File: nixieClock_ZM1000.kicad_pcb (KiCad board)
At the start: 2 copper layers, 124.5 x 100.3 mm, 62 parts, among them J1 Conn_01x08_Female, J2 Conn_01x02_Female, J3 SPARE, Q1 BC547, Q2 BC547, Q3 BC547, Q4 BC547, Q5 BC547, Q6 BC547, Q7 Q_NMOS_GDS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

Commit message: 90% routed
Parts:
- moved J3 13.5 mm to (192.5, 113.8)
- moved R8 10.2 mm to (121.7, 82.5), turned to 90 degrees
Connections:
- U14 pad 1: /Shift Registers/BCD_T1B -> /Shift Registers/DP1
- U14 pad 15: /Shift Registers/BCD_T1A -> /Shift Registers/BCD_T2C
- U14 pad 2: /Shift Registers/BCD_T1C -> /Shift Registers/BCD_T1A
- U14 pad 4: /Shift Registers/DP1 -> /Shift Registers/BCD_T1B
- U14 pad 5: /Shift Registers/BCD_T2A -> /Shift Registers/BCD_T1C
- U14 pad 6: /Shift Registers/BCD_T2B -> /Shift Registers/BCD_T2A
- U14 pad 7: /Shift Registers/BCD_T2C -> /Shift Registers/BCD_T2B
- U15 pad 15: /Shift Registers/BCD_T2D -> /Shift Registers/BCD_T4A
- U15 pad 2: /Shift Registers/BCD_T3A -> /Shift Registers/BCD_T2D
- U15 pad 3: /Shift Registers/BCD_T3B -> /Shift Registers/BCD_T3C
- U15 pad 4: /Shift Registers/BCD_T3C -> /Shift Registers/BCD_T3B
- U15 pad 6: /Shift Registers/DP3 -> /Shift Registers/BCD_T3A
- U15 pad 7: /Shift Registers/BCD_T4A -> /Shift Registers/DP3
- U16 pad 1: /Shift Registers/BCD_T4C -> /Shift Registers/DP4
- U16 pad 15: /Shift Registers/BCD_T4B -> /Shift Registers/BCD_T5A
- U16 pad 3: /Shift Registers/DP4 -> /Shift Registers/BCD_T4B
- U16 pad 4: /Shift Registers/BCD_T5A -> /Shift Registers/BCD_T4C
- U16 pad 5: /Shift Registers/BCD_T5B -> /Shift Registers/BCD_T5C
- U16 pad 6: /Shift Registers/BCD_T5C -> /Shift Registers/BCD_T5B
- U17 pad 1: /Shift Registers/BCD_T6A -> /Shift Registers/DP5
- U17 pad 15: /Shift Registers/DP5 -> /Shift Registers/DP6
- U17 pad 2: /Shift Registers/BCD_T6B -> /Shift Registers/BCD_T6C
- U17 pad 3: /Shift Registers/BCD_T6C -> /Shift Registers/BCD_T6B
- U17 pad 5: /Shift Registers/DP6 -> /Shift Registers/BCD_T6A
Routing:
- net /Control/BLANK: track 45.8 -> 160.5 mm
- net /Control/5V: track 15.0 -> 128.7 mm, vias 0 -> 1
- net Net-(U2-Pad5): track 0.00 -> 51.2 mm
- net Net-(U4-Pad5): track 0.00 -> 51.2 mm
- net Net-(U10-Pad5): track 0.00 -> 51.2 mm
- net Net-(U3-Pad5): track 0.00 -> 51.2 mm
- net /PSU/HV: track 0.00 -> 51.1 mm
- net Net-(U11-Pad8): track 0.00 -> 51.1 mm
- net Net-(U12-Pad8): track 0.00 -> 51.0 mm
- net /Shift Registers/BCD_T4A: track 0.00 -> 40.3 mm
- net /Shift Registers/BCD_T2A: track 0.00 -> 39.6 mm
- net /Shift Registers/BCD_T5D: track 0.00 -> 37.1 mm
- net /Shift Registers/BCD_T2D: track 0.00 -> 36.5 mm
- net Net-(U12-Pad1): track 0.00 -> 36.1 mm
- net Net-(U3-Pad11): track 0.00 -> 36.1 mm
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- added copper zone on B.Cu, net GND

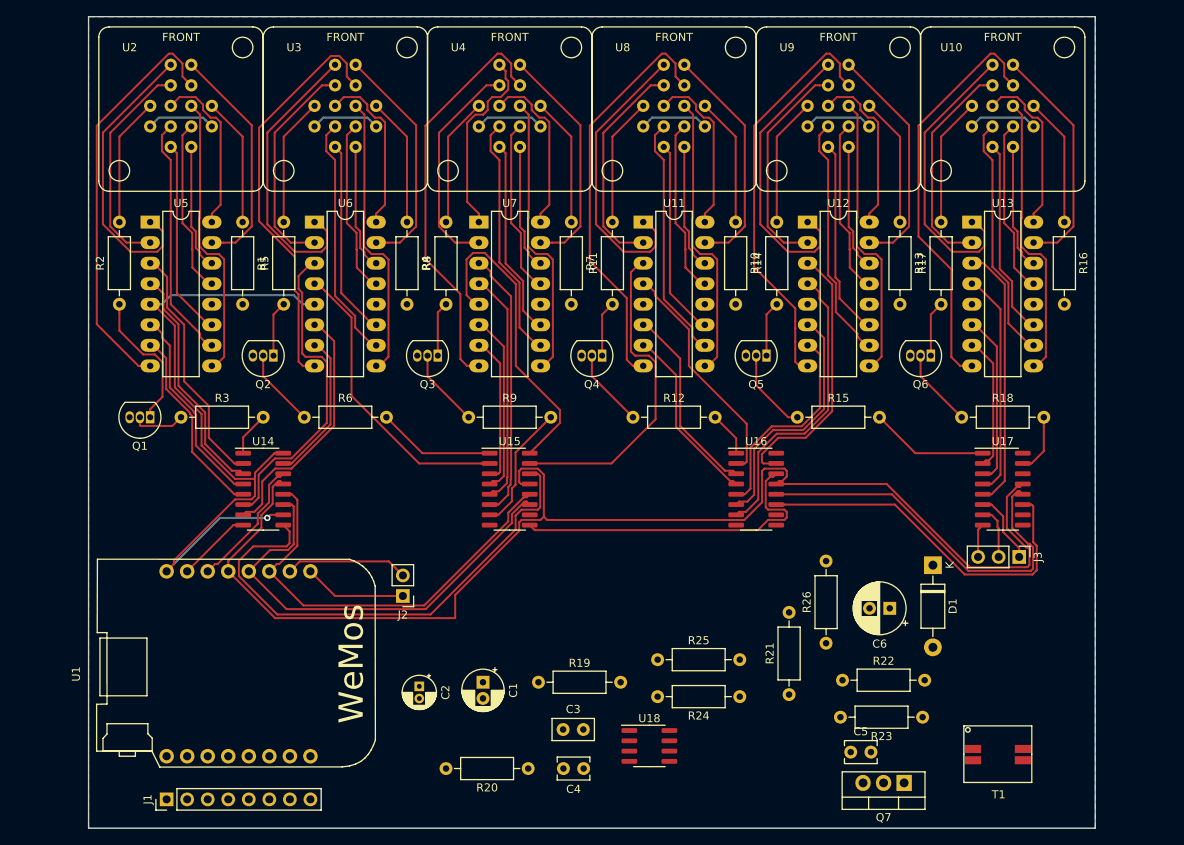
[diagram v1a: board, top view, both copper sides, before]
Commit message: Completed layout inc optimisation of data pattern for shift registers
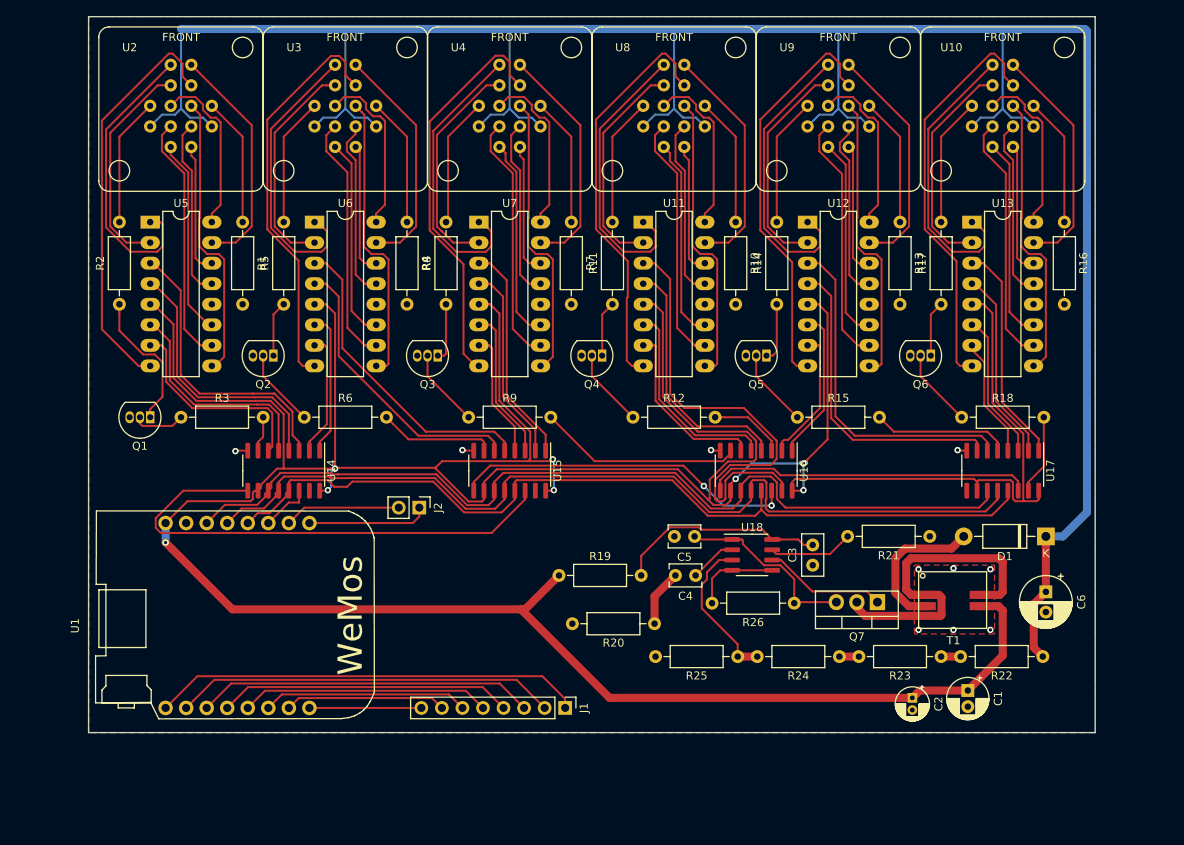
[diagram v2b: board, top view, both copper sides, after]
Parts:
- removed J3: SPARE, Connector_PinHeader_2.54mm:PinHeader_1x03_P2.54mm_Vertical
- moved C2 61.0 mm to (179.3, 131.2)
- moved C1 60.0 mm to (186.2, 130.3)
- moved J1 50.6 mm to (136.4, 132.5), turned to 270 degrees
- moved C3 37.0 mm to (167.0, 114.8), turned to 90 degrees
- moved C5 32.9 mm to (152.4, 111.3), turned to 180 degrees
- moved C4 27.6 mm to (152.5, 116.1)
- moved U18 26.8 mm to (159.5, 113.5)
- moved R21 26.2 mm to (181.5, 111.3), turned to 180 degrees
- moved R22 24.9 mm to (195.5, 126.1), turned to 180 degrees
- moved R20 23.8 mm to (147.4, 122.0)
- moved Q7 22.6 mm to (175.0, 119.4)
- moved T1 19.9 mm to (184.4, 119.1)
- moved C6 19.4 mm to (195.8, 118.1), turned to 270 degrees
- moved D1 14.4 mm to (195.8, 111.3), turned to 180 degrees
- moved R19 13.5 mm to (135.6, 116.1)
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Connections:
- U1 pad 3: /Control/TUBETX -> /Control/SHIFTCLK
- U1 pad 4: /Control/BLANK -> /Control/STORAGECLK
- U1 pad 5: /Control/SHIFTCLK -> /Control/BLANK
- U1 pad 6: /Control/STORAGECLK -> /Control/TUBETX
- U14 pad 1: /Shift Registers/DP1 -> /Shift Registers/BCD_T2B
- U14 pad 15: /Shift Registers/BCD_T2C -> Net-(U14-Pad15)
- U14 pad 2: /Shift Registers/BCD_T1A -> /Shift Registers/BCD_T2C
- U14 pad 3: /Shift Registers/BCD_T1D -> /Shift Registers/BCD_T1A
- U14 pad 4: /Shift Registers/BCD_T1B -> /Shift Registers/BCD_T1D
- U14 pad 5: /Shift Registers/BCD_T1C -> /Shift Registers/BCD_T1B
- U14 pad 6: /Shift Registers/BCD_T2A -> /Shift Registers/BCD_T1C
- U14 pad 7: /Shift Registers/BCD_T2B -> /Shift Registers/DP1
- U15 pad 1: /Shift Registers/DP2 -> /Shift Registers/BCD_T3A
- U15 pad 15: /Shift Registers/BCD_T4A -> Net-(U15-Pad15)
- U15 pad 2: /Shift Registers/BCD_T2D -> /Shift Registers/BCD_T3D
- U15 pad 3: /Shift Registers/BCD_T3C -> /Shift Registers/BCD_T3B
- U15 pad 4: /Shift Registers/BCD_T3B -> /Shift Registers/BCD_T3C
- U15 pad 5: /Shift Registers/BCD_T3D -> /Shift Registers/BCD_T2A
- U15 pad 6: /Shift Registers/BCD_T3A -> /Shift Registers/BCD_T2D
- U15 pad 7: /Shift Registers/DP3 -> /Shift Registers/DP2
- U16 pad 1: /Shift Registers/DP4 -> /Shift Registers/BCD_T5B
- U16 pad 15: /Shift Registers/BCD_T5A -> /Shift Registers/BCD_T4A
- U16 pad 2: /Shift Registers/BCD_T4D -> /Shift Registers/BCD_T5C
- U16 pad 3: /Shift Registers/BCD_T4B -> /Shift Registers/DP4
- U16 pad 4: /Shift Registers/BCD_T4C -> /Shift Registers/BCD_T4D
- U16 pad 5: /Shift Registers/BCD_T5C -> /Shift Registers/BCD_T4B
- U16 pad 6: /Shift Registers/BCD_T5B -> /Shift Registers/BCD_T4C
- U16 pad 7: /Shift Registers/BCD_T5D -> /Shift Registers/DP3
- U17 pad 1: /Shift Registers/DP5 -> /Shift Registers/BCD_T6A
- U17 pad 2: /Shift Registers/BCD_T6C -> /Shift Registers/BCD_T6D
- U17 pad 4: /Shift Registers/BCD_T6D -> /Shift Registers/BCD_T6C
- U17 pad 5: /Shift Registers/BCD_T6A -> /Shift Registers/DP5
- U17 pad 6: Net-(J3-Pad1) -> /Shift Registers/BCD_T5A
- U17 pad 7: Net-(J3-Pad2) -> /Shift Registers/BCD_T5D
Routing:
- net /Control/5V: track 128.7 -> 455.9 mm, vias 1 -> 8
- net /PSU/HV: track 51.1 -> 309.6 mm
- net Net-(J1-Pad1): track 0.00 -> 53.3 mm
- net /Control/BLANK: track 160.5 -> 108.8 mm
- net Net-(J1-Pad2): track 0.00 -> 47.2 mm
- net Net-(J1-Pad3): track 0.00 -> 41.7 mm
- net Net-(Q7-Pad2): track 0.00 -> 41.1 mm
- net Net-(U16-Pad9): track 0.00 -> 40.5 mm
- net Net-(J1-Pad4): track 0.00 -> 36.3 mm
- net Net-(J1-Pad5): track 0.00 -> 30.8 mm
- net Net-(C3-Pad2): track 0.00 -> 26.0 mm
- net Net-(J1-Pad6): track 0.00 -> 25.4 mm
- net Net-(C5-Pad1): track 0.00 -> 23.0 mm
- net Net-(J1-Pad7): track 0.00 -> 19.9 mm
- net /Shift Registers/BCD_T4A: track 40.3 -> 59.9 mm
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- added copper zone on F.Cu, net GND
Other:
- board size 124.5 x 100.3 mm -> 124.5 x 88.5 mm

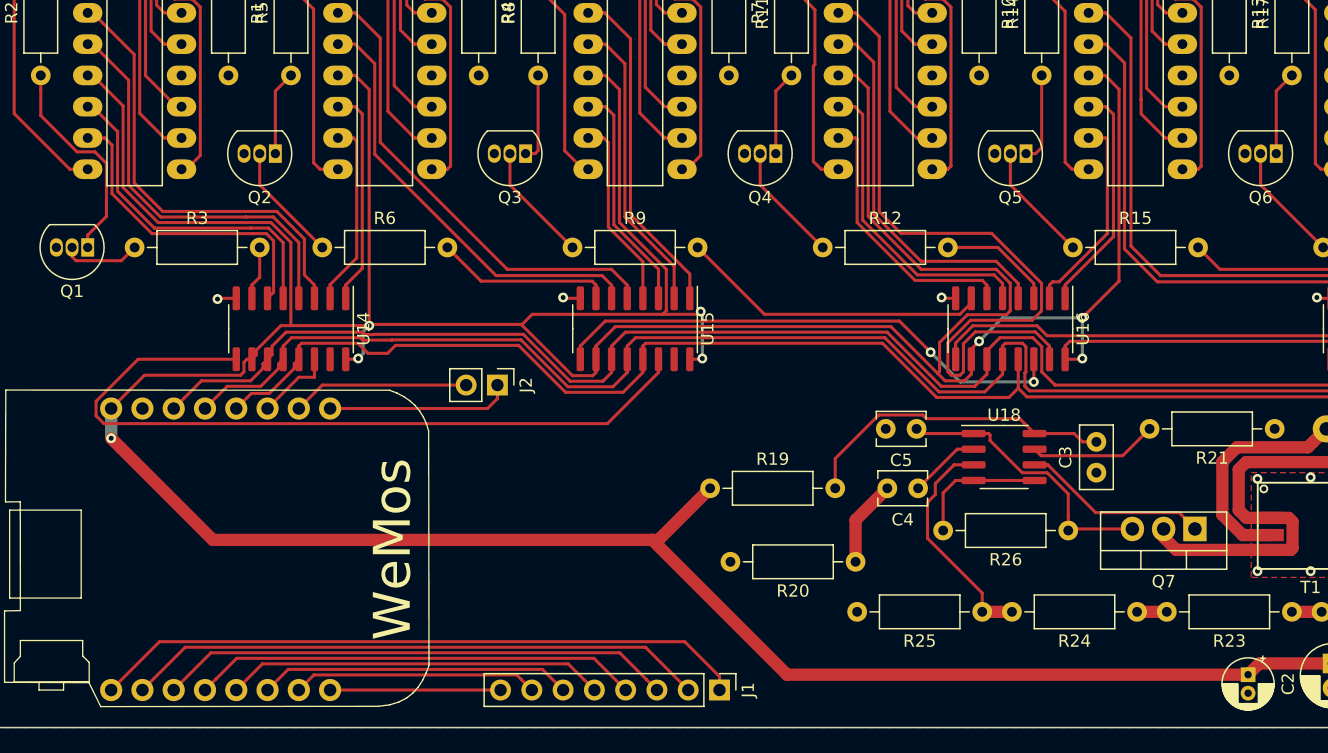
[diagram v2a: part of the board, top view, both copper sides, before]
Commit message: Added more decoupling
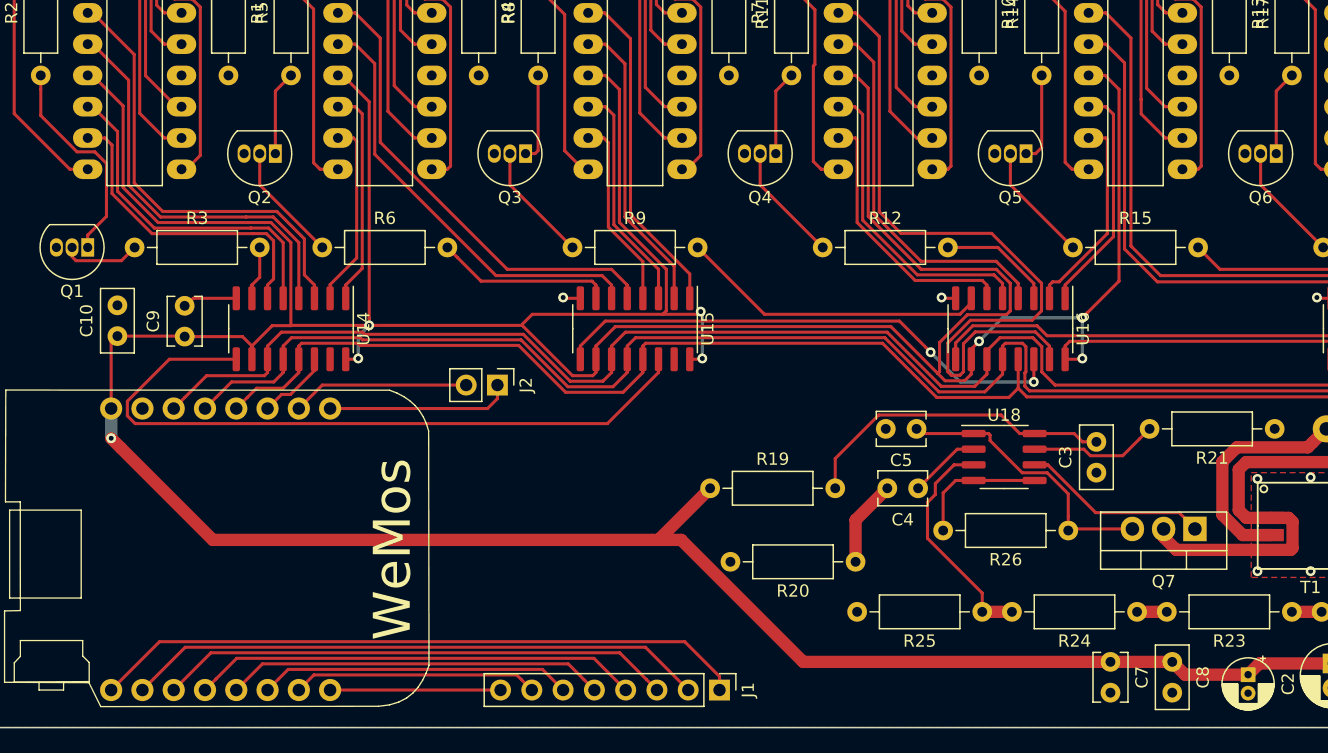
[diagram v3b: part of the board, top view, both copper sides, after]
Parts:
- added C10: 100n, Capacitor_THT:C_Disc_D5.0mm_W2.5mm_P2.50mm, F.Cu at (87.5, 103.7)
- added C7: 10n, Capacitor_THT:C_Disc_D3.8mm_W2.6mm_P2.50mm, F.Cu at (168.1, 130.2)
- added C8: 100n, Capacitor_THT:C_Disc_D5.0mm_W2.5mm_P2.50mm, F.Cu at (173.2, 130.2)
- added C9: 10n, Capacitor_THT:C_Disc_D3.8mm_W2.6mm_P2.50mm, F.Cu at (93.0, 103.8)
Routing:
- net Net-(U14-Pad9): track 62.7 -> 57.6 mm
- net /Control/5V: track 455.9 -> 460.0 mm
- net GND: track 16.2 -> 19.1 mm, vias 10 -> 9
- net /Control/SHIFTCLK: track 113.2 -> 113.8 mm

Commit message: Update to PSU
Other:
- outline, holes or cut-outs redrawn
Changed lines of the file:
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@@
   )
   (setup
-    (last_trace_width 1)
+    (last_trace_width 0.25)
     (user_trace_width 1)
     (trace_clearance 0.2)
@@
   )
   (gr_line (start 77.47 135.509) (end 201.93 135.509) (layer Edge.Cuts) (width 0.12))
-  (gr_line (start 77.47 46.99) (end 77.47 135.509) (layer Edge.Cuts) (width 0.12))
+  (gr_line (start 77.47 46.99) (end 77.47 133.985) (layer Edge.Cuts) (width 0.12))
   (gr_line (start 201.93 46.99) (end 201.93 135.509) (layer Edge.Cuts) (width 0.12))
   (gr_line (start 77.47 46.99) (end 201.93 46.99) (layer Edge.Cuts) (width 0.12))
@@
   (zone (net 2) (net_name GND) (layer B.Cu) (hatch edge 0.508)
     (connect_pads thru_hole_only (clearance 0.508))
-    (min_thickness 0.254)
+    (min_thickness 0.127)
     (fill yes (arc_segments 32) (thermal_gap 0.508) (thermal_bridge_width 0.508))
     (polygon

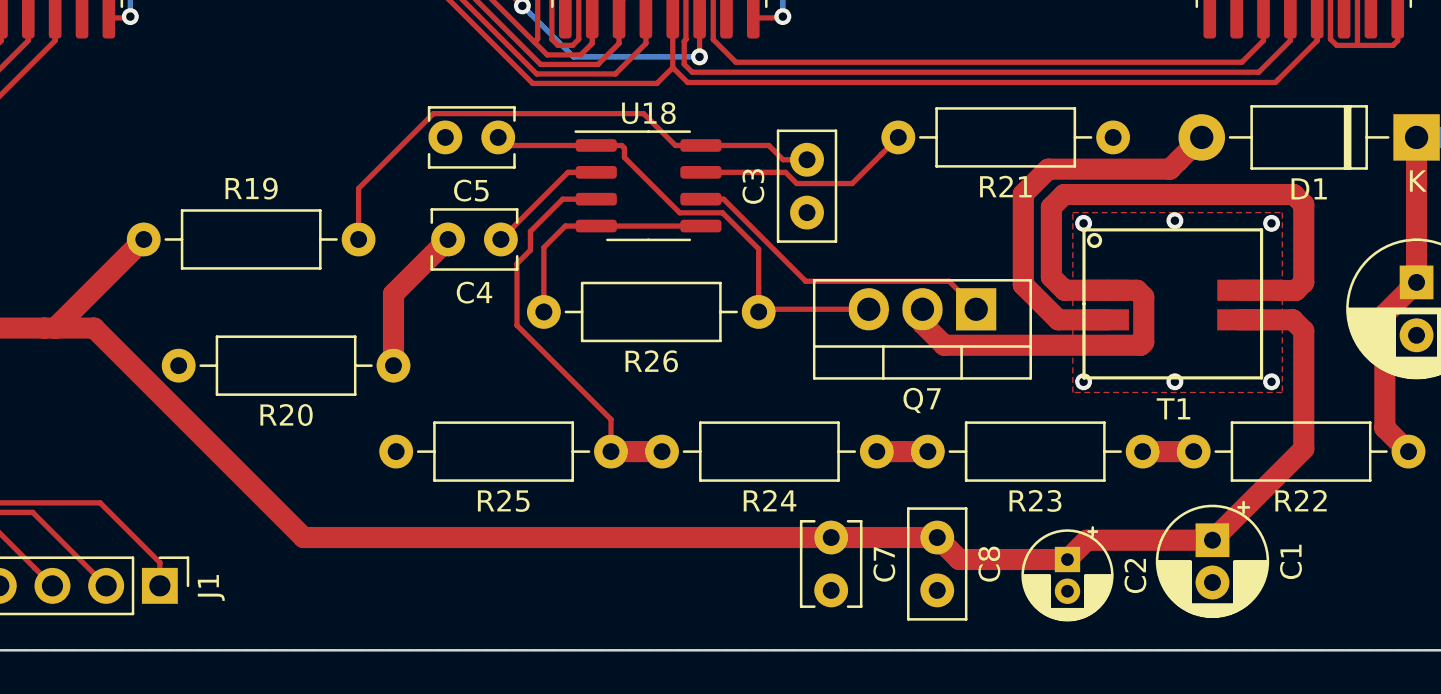
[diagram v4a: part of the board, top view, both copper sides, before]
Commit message: Corrected errors on PSU
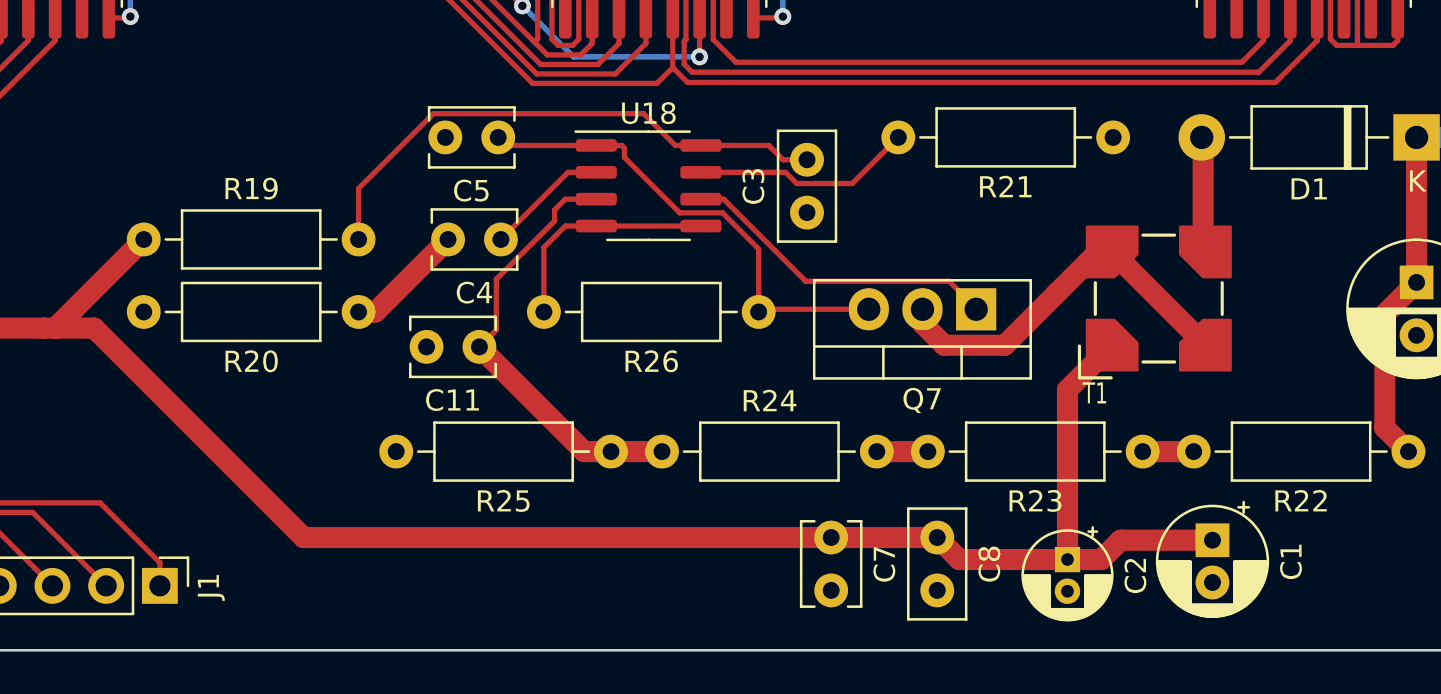
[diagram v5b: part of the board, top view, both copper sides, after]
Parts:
- added C11: 1n, Capacitor_THT:C_Disc_D3.8mm_W2.6mm_P2.50mm, F.Cu at (151.5, 121.2)
- C3: value 0.1u -> 100n
- C4: value 22n -> 100n
- C5: value 0.01u -> 10n
- R20: value 4k7 -> 1k
- R21: value 15k -> 220k
- T1: footprint BamboulabFootprints:CTX02-18714-R -> BamboulabFootprints:Transformer_LPR6235
- moved R24 10.2 mm to (160.1, 126.1), turned to 0 degrees
- moved R20 3.03 mm to (145.8, 119.5)
- moved T1 0.80 mm to (183.6, 118.9)
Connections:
- R22 pad 1: /PSU/HV -> Net-(R22-Pad1)
- R22 pad 2: Net-(R22-Pad2) -> /PSU/HV
- R23 pad 1: Net-(R22-Pad2) -> Net-(R22-Pad1)
- R24 pad 1: Net-(R23-Pad2) -> Net-(C11-Pad1)
- R24 pad 2: Net-(R24-Pad2) -> Net-(R23-Pad2)
- R25 pad 1: Net-(R24-Pad2) -> Net-(C11-Pad1)
- T1 pad 1: Net-(Q7-Pad2) -> /Control/5V
- T1 pad 2: Net-(D1-Pad2) -> Net-(Q7-Pad2)
- T1 pad 3: /Control/5V -> Net-(D1-Pad2)
- U18 pad 3: Net-(R24-Pad2) -> Net-(C11-Pad1)
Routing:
- net Net-(Q7-Pad2): track 41.1 -> 18.9 mm
- net Net-(C11-Pad1): track 0.00 -> 20.8 mm
- net Net-(R24-Pad2): track 18.7 -> 0.00 mm
- net Net-(D1-Pad2): track 18.5 -> 5.55 mm
- net /Control/5V: track 460.0 -> 456.2 mm
- net Net-(C4-Pad2): track 7.04 -> 5.65 mm
- net GND: vias 9 -> 3
- removed copper zone on F.Cu, net GND
